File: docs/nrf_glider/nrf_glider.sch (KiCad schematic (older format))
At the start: 25 parts

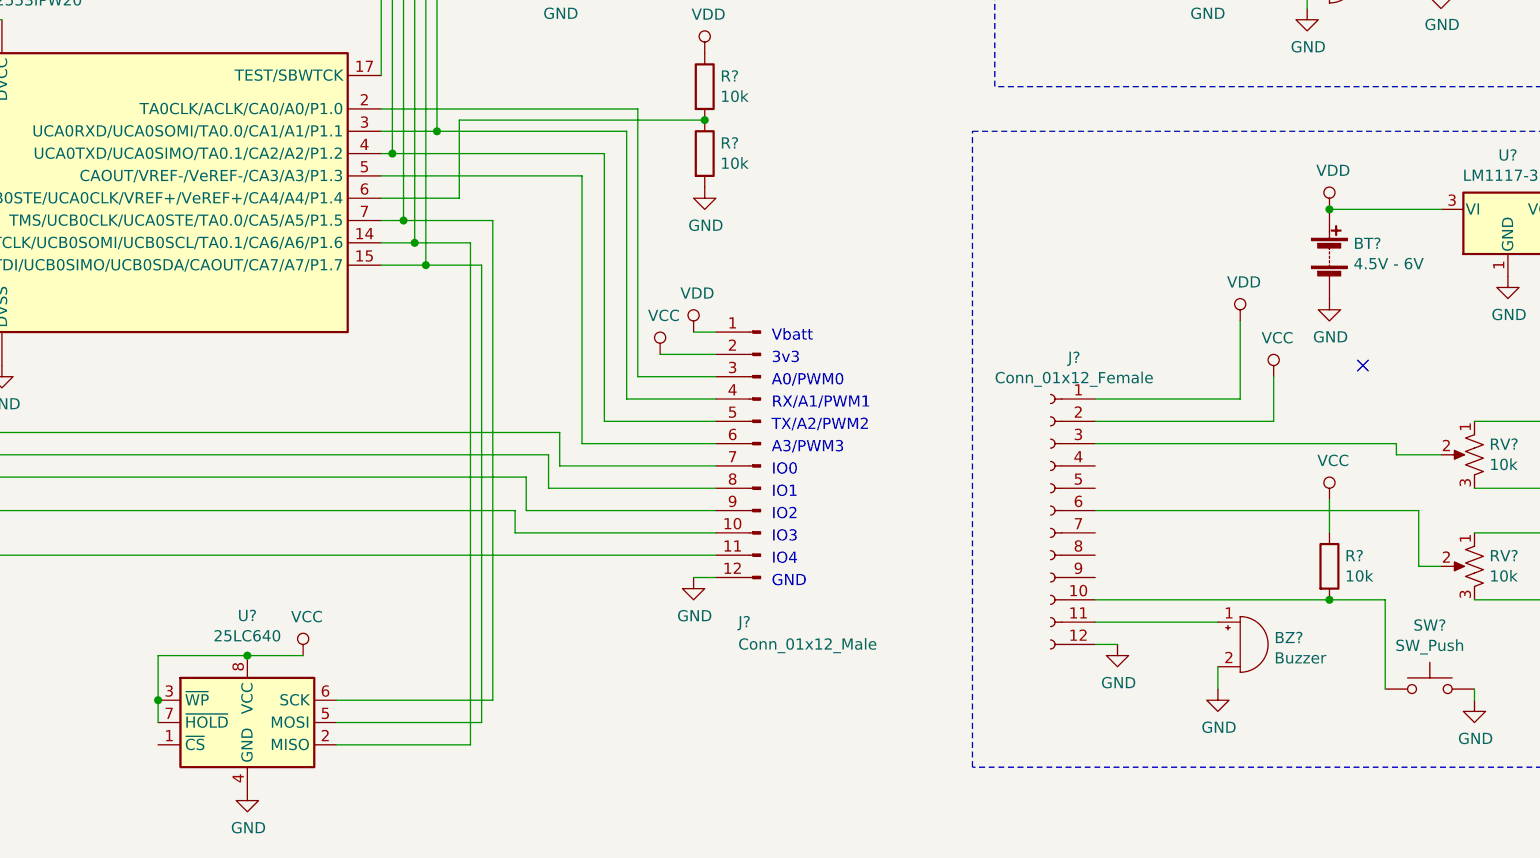
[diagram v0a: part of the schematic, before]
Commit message: add CS for eeprom, add UART connector on TX module
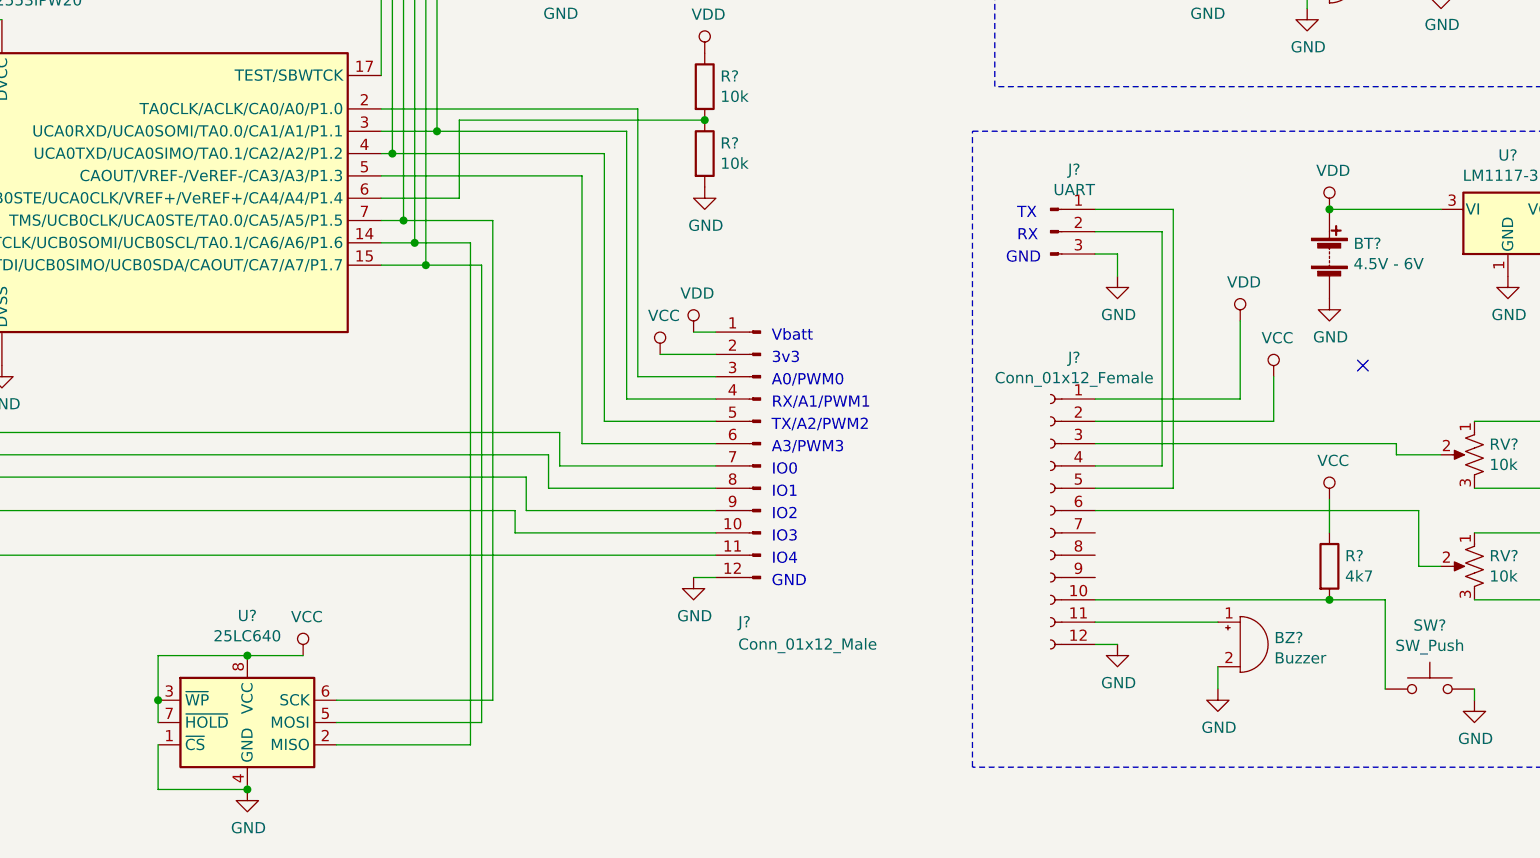
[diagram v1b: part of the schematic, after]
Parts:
- added J?: UART, symbol Connector:Conn_01x03_Male
- R?: value 10k -> 4k7
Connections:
- net GND: now also U?.1 (~CS), J?.3 (Pin_3)
- net at J?.4 (Pin_4): now also J?.2 (Pin_2)
- net at J?.5 (Pin_5): now also J?.1 (Pin_1)
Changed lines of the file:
@@
 EESchema Schematic File Version 4
+LIBS:nrf_glider-cache
 EELAYER 26 0
 EELAYER END
@@
 P 8800 5550
 F 0 "R?" H 8870 5596 50  0000 L CNN
-F 1 "10k" H 8870 5505 50  0000 L CNN
+F 1 "4k7" H 8870 5505 50  0000 L CNN
 F 2 "" V 8730 5550 50  0001 C CNN
 F 3 "~" H 8800 5550 50  0001 C CNN
@@
 Wire Wire Line
 	8800 5250 8800 5400
+$Comp
+L Connector:Conn_01x03_Male J?
+U 1 1 5BCF8F2B
+P 7550 4050
+F 0 "J?" H 7656 4328 50  0000 C CNN
+F 1 "UART" H 7656 4237 50  0000 C CNN
+F 2 "" H 7550 4050 50  0001 C CNN
+F 3 "~" H 7550 4050 50  0001 C CNN
+	1    7550 4050
+	1    0    0    -1
+$EndComp
+Wire Wire Line
+	7750 5100 8050 5100
+Wire Wire Line
+	8050 5100 8050 4050
+Wire Wire Line
+	8050 4050 7750 4050
+Wire Wire Line
+	7750 3950 8100 3950
+Wire Wire Line
+	8100 3950 8100 5200
+Wire Wire Line
+	8100 5200 7750 5200
+$Comp
+L power:GND #PWR?
+U 1 1 5BD038ED
+P 7850 4250
+F 0 "#PWR?" H 7850 4000 50  0001 C CNN
+F 1 "GND" H 7855 4077 50  0000 C CNN
+F 2 "" H 7850 4250 50  0001 C CNN
+F 3 "" H 7850 4250 50  0001 C CNN
+	1    7850 4250
+	1    0    0    -1
+$EndComp
+Wire Wire Line
+	7750 4150 7850 4150
+Wire Wire Line
+	7850 4150 7850 4250
+Text Notes 7400 4000 0    50   ~ 0
+TX
+Text Notes 7400 4100 0    50   ~ 0
+RX
+Text Notes 7350 4200 0    50   ~ 0
+GND
+Wire Wire Line
+	3550 6350 3550 6550
+Wire Wire Line
+	3550 6550 3950 6550
+Connection ~ 3950 6550
 $EndSCHEMATC

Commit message: tweaks to schematic
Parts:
- BT1, BT2: renamed from BT?; value 4.5V - 6V -> 4.5V - 9.9V
- M1: renamed from M?; value Motor_Servo -> Servo Left
- M2: renamed from M?; value Motor_Servo -> Servo Right
- R1: renamed from R?; value 10k -> 20k
- SW1: renamed from SW?; value SW_Push -> TRIM
- gave numbers to parts that had none: 20
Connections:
- net GND: no longer U2.1 (~CS)
- net at J2.7 (Pin_7), U1.18 (P2.7/XOUT): now also U2.1 (~CS)
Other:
- note added: "* IO0 shared with EEPROM chip select"
- note added: "23 October 2018"
- note added: "IO0*"
- note added: "Joystick"
- note added: "Left/Right\n"
- note added: "NRF and MSP430 based RC control"
- note added: "Up/Down"
- note added: "created by Toby Kurien"
- note removed: "IO0"
- moved on the sheet: R3

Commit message: added switch
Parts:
- added SW?: SW_SPST, symbol Switch:SW_SPST
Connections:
- net VDD: now also SW?.2 (B); no longer BT1.1 (+)
- new net: BT1.1 (+), SW?.1 (A)
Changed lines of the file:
@@
 	1    0    0    -1
 $EndComp
-Wire Wire Line
-	8800 3950 9300 3950
 $Comp
 L power:GND #PWR025
@@
 L power:VDD #PWR024
 U 1 1 5BD2C8A2
-P 8800 3950
-F 0 "#PWR024" H 8800 3800 50  0001 C CNN
-F 1 "VDD" H 8817 4123 50  0000 C CNN
-F 2 "" H 8800 3950 50  0001 C CNN
-F 3 "" H 8800 3950 50  0001 C CNN
-	1    8800 3950
-	1    0    0    -1
-$EndComp
-Connection ~ 8800 3950
+P 9300 3850
+F 0 "#PWR024" H 9300 3700 50  0001 C CNN
+F 1 "VDD" H 9317 4023 50  0000 C CNN
+F 2 "" H 9300 3850 50  0001 C CNN
+F 3 "" H 9300 3850 50  0001 C CNN
+	1    9300 3850
+	1    0    0    -1
+$EndComp
 Wire Wire Line
 	10450 3950 10450 4000
@@
 	8500 5700 9050 5700
 Wire Wire Line
-	3950 5950 4200 5950
-Wire Wire Line
-	3550 5950 3950 5950
-Connection ~ 3950 5950
-Connection ~ 3550 6150
-Wire Wire Line
-	3550 6150 3550 5950
-Wire Wire Line
-	3550 6250 3550 6150
-Wire Wire Line
 	3550 6350 1150 6350
 Wire Wire Line
@@
 Text Notes 10300 7350 0    50   ~ 0
 created by Toby Kurien
+$Comp
+L Switch:SW_SPST SW?
+U 1 1 5BD0D3D1
+P 9000 3950
+F 0 "SW?" H 9000 4185 50  0000 C CNN
+F 1 "SW_SPST" H 9000 4094 50  0000 C CNN
+F 2 "" H 9000 3950 50  0001 C CNN
+F 3 "" H 9000 3950 50  0001 C CNN
+	1    9000 3950
+	1    0    0    -1
+$EndComp
+Wire Wire Line
+	9200 3950 9300 3950
+Wire Wire Line
+	9300 3850 9300 3950
+Connection ~ 9300 3950
+Wire Wire Line
+	3550 6250 3550 6150
+Wire Wire Line
+	3550 6150 3550 5950
+Connection ~ 3550 6150
+Connection ~ 3950 5950
+Wire Wire Line
+	3550 5950 3950 5950
+Wire Wire Line
+	3950 5950 4200 5950
 $EndSCHEMATC

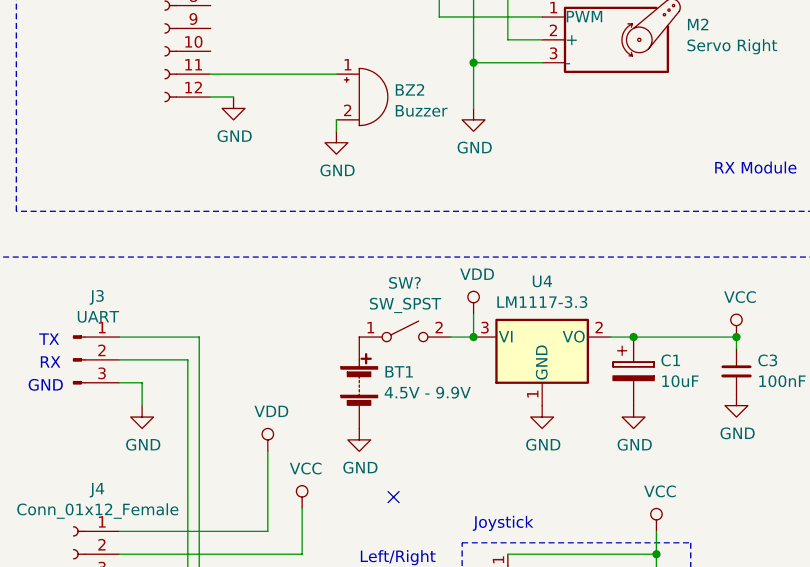
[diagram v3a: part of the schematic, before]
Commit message: Added some footprints
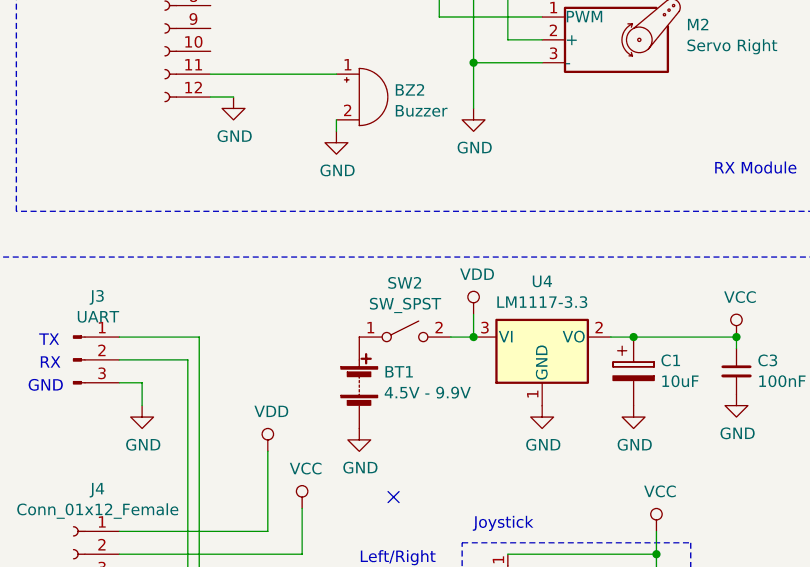
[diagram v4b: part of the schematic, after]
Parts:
- BT1, BT2: footprint (none) -> Connector_PinHeader_2.54mm:PinHeader_1x02_P2.54mm_Vertical
- BZ1, BZ2: footprint (none) -> Buzzer_Beeper:Buzzer_15x7.5RM7.6
- C1, C2: footprint (none) -> Capacitor_THT:CP_Radial_D8.0mm_P2.50mm
- C3, C4: footprint (none) -> Capacitor_THT:C_Disc_D5.0mm_W2.5mm_P5.00mm
- J1: footprint (none) -> Connector_PinHeader_2.54mm:PinHeader_1x06_P2.54mm_Vertical
- J2, J4, J5: footprint (none) -> Connector_PinHeader_2.54mm:PinHeader_1x12_P2.54mm_Vertical
- J3: footprint (none) -> Connector_PinHeader_2.54mm:PinHeader_1x03_P2.54mm_Horizontal
- M1, M2: footprint (none) -> Connector_PinHeader_2.54mm:PinHeader_1x03_P2.54mm_Vertical
- R1, R2, R3: footprint (none) -> Resistor_THT:R_Axial_DIN0411_L9.9mm_D3.6mm_P12.70mm_Horizontal
- RV1, RV2: footprint (none) -> Potentiometer_THT:Potentiometer_ACP_CA9-V10_Vertical
- SW1: footprint (none) -> Button_Switch_THT:SW_PUSH_6mm_H5mm
- U1: footprint Package_SO:TSSOP-20_4.4x6.5mm_P0.65mm -> Package_DIP:DIP-20_W7.62mm
- U2: footprint (none) -> Package_DIP:DIP-8_W7.62mm
- gave numbers to parts that had none: 1
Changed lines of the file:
@@
 F 0 "U1" H 2850 4878 50  0000 C CNN
 F 1 "MSP430G2553IPW20" H 2850 4787 50  0000 C CNN
-F 2 "Package_SO:TSSOP-20_4.4x6.5mm_P0.65mm" H 1400 3350 50  0001 C CIN
+F 2 "Package_DIP:DIP-20_W7.62mm" H 1400 3350 50  0001 C CIN
 F 3 "http://www.ti.com/lit/ds/symlink/msp430g2553.pdf" H 2800 3900 50  0001 C CNN
 	1    2850 3900
@@
 F 0 "U2" H 3950 6728 50  0000 C CNN
 F 1 "25LC640" H 3950 6637 50  0000 C CNN
-F 2 "" H 3950 6250 50  0001 C CNN
+F 2 "Package_DIP:DIP-8_W7.62mm" H 3950 6250 50  0001 C CNN
 F 3 "http://ww1.microchip.com/downloads/en/DeviceDoc/21832H.pdf" H 3950 6250 50  0001 C CNN
 	1    3950 6250
@@
 F 0 "BT2" H 9058 1246 50  0000 L CNN
 F 1 "4.5V - 9.9V" H 9058 1155 50  0000 L CNN
-F 2 "" V 8950 1260 50  0001 C CNN
+F 2 "Connector_PinHeader_2.54mm:PinHeader_1x02_P2.54mm_Vertical" V 8950 1260 50  0001 C CNN
 F 3 "~" V 8950 1260 50  0001 C CNN
 	1    8950 1200
@@
 F 0 "C4" H 10692 1196 50  0000 L CNN
 F 1 "100nF" H 10692 1105 50  0000 L CNN
-F 2 "" H 10600 1150 50  0001 C CNN
+F 2 "Capacitor_THT:C_Disc_D5.0mm_W2.5mm_P5.00mm" H 10600 1150 50  0001 C CNN
 F 3 "~" H 10600 1150 50  0001 C CNN
 	1    10600 1150
@@
 F 0 "C2" H 10268 1196 50  0000 L CNN
 F 1 "10uF" H 10268 1105 50  0000 L CNN
-F 2 "" H 10188 1000 50  0001 C CNN
+F 2 "Capacitor_THT:CP_Radial_D8.0mm_P2.50mm" H 10188 1000 50  0001 C CNN
 F 3 "~" H 10150 1150 50  0001 C CNN
 	1    10150 1150
@@
 F 0 "R1" H 6070 3446 50  0000 L CNN
 F 1 "20k" H 6070 3355 50  0000 L CNN
-F 2 "" V 5930 3400 50  0001 C CNN
+F 2 "Resistor_THT:R_Axial_DIN0411_L9.9mm_D3.6mm_P12.70mm_Horizontal" V 5930 3400 50  0001 C CNN
 F 3 "~" H 6000 3400 50  0001 C CNN
 	1    6000 3400
@@
 F 0 "R2" H 6070 3746 50  0000 L CNN
 F 1 "10k" H 6070 3655 50  0000 L CNN
-F 2 "" V 5930 3700 50  0001 C CNN
+F 2 "Resistor_THT:R_Axial_DIN0411_L9.9mm_D3.6mm_P12.70mm_Horizontal" V 5930 3700 50  0001 C CNN
 F 3 "~" H 6000 3700 50  0001 C CNN
 	1    6000 3700
@@
 F 0 "J2" H 6350 4200 50  0000 R CNN
 F 1 "Conn_01x12_Male" H 6350 4100 50  0000 R CNN
-F 2 "" H 6250 5000 50  0001 C CNN
+F 2 "Connector_PinHeader_2.54mm:PinHeader_1x12_P2.54mm_Vertical" H 6250 5000 50  0001 C CNN
 F 3 "~" H 6250 5000 50  0001 C CNN
 	1    6250 5000
@@
 F 0 "J5" H 7844 2985 50  0000 C CNN
 F 1 "Conn_01x12_Female" H 7844 2894 50  0000 C CNN
-F 2 "" H 7950 2300 50  0001 C CNN
+F 2 "Connector_PinHeader_2.54mm:PinHeader_1x12_P2.54mm_Vertical" H 7950 2300 50  0001 C CNN
 F 3 "~" H 7950 2300 50  0001 C CNN
 	1    7950 2300
@@
 F 0 "J4" H 7444 5985 50  0000 C CNN
 F 1 "Conn_01x12_Female" H 7444 5894 50  0000 C CNN
-F 2 "" H 7550 5300 50  0001 C CNN
+F 2 "Connector_PinHeader_2.54mm:PinHeader_1x12_P2.54mm_Vertical" H 7550 5300 50  0001 C CNN
 F 3 "~" H 7550 5300 50  0001 C CNN
 	1    7550 5300
@@
 F 0 "M1" H 10231 2215 50  0000 L CNN
 F 1 "Servo Left" H 10231 2124 50  0000 L CNN
-F 2 "" H 9900 1960 50  0001 C CNN
+F 2 "Connector_PinHeader_2.54mm:PinHeader_1x03_P2.54mm_Vertical" H 9900 1960 50  0001 C CNN
 F 3 "http://forums.parallax.com/uploads/attachments/46831/74481.png" H 9900 1960 50  0001 C CNN
 	1    9900 2150
@@
 F 0 "M2" H 10231 2715 50  0000 L CNN
 F 1 "Servo Right" H 10231 2624 50  0000 L CNN
-F 2 "" H 9900 2460 50  0001 C CNN
+F 2 "Connector_PinHeader_2.54mm:PinHeader_1x03_P2.54mm_Vertical" H 9900 2460 50  0001 C CNN
 F 3 "http://forums.parallax.com/uploads/attachments/46831/74481.png" H 9900 2460 50  0001 C CNN
 	1    9900 2650
@@
 F 0 "BZ2" H 8953 2929 50  0000 L CNN
 F 1 "Buzzer" H 8953 2838 50  0000 L CNN
-F 2 "" V 8775 3000 50  0001 C CNN
+F 2 "Buzzer_Beeper:Buzzer_15x7.5RM7.6" V 8775 3000 50  0001 C CNN
 F 3 "~" V 8775 3000 50  0001 C CNN
 	1    8800 2900
@@
 F 0 "RV1" H 9383 5096 50  0000 R CNN
 F 1 "10k" H 9383 5005 50  0000 R CNN
-F 2 "" H 9450 5050 50  0001 C CNN
+F 2 "Potentiometer_THT:Potentiometer_ACP_CA9-V10_Vertical" H 9450 5050 50  0001 C CNN
 F 3 "~" H 9450 5050 50  0001 C CNN
 	1    9450 5050
@@
 F 0 "RV2" H 9383 5596 50  0000 R CNN
 F 1 "10k" H 9383 5505 50  0000 R CNN
-F 2 "" H 9450 5550 50  0001 C CNN
+F 2 "Potentiometer_THT:Potentiometer_ACP_CA9-V10_Vertical" H 9450 5550 50  0001 C CNN
 F 3 "~" H 9450 5550 50  0001 C CNN
 	1    9450 5550
@@
 F 0 "BZ1" H 8553 5929 50  0000 L CNN
 F 1 "Buzzer" H 8553 5838 50  0000 L CNN
-F 2 "" V 8375 6000 50  0001 C CNN
+F 2 "Buzzer_Beeper:Buzzer_15x7.5RM7.6" V 8375 6000 50  0001 C CNN
 F 3 "~" V 8375 6000 50  0001 C CNN
 	1    8400 5900
@@
 F 0 "SW1" H 9250 6385 50  0000 C CNN
 F 1 "TRIM" H 9250 6294 50  0000 C CNN
-F 2 "" H 9250 6300 50  0001 C CNN
+F 2 "Button_Switch_THT:SW_PUSH_6mm_H5mm" H 9250 6300 50  0001 C CNN
 F 3 "" H 9250 6300 50  0001 C CNN
 	1    9250 6100
@@
 F 0 "BT1" H 8908 4196 50  0000 L CNN
 F 1 "4.5V - 9.9V" H 8908 4105 50  0000 L CNN
-F 2 "" V 8800 4210 50  0001 C CNN
+F 2 "Connector_PinHeader_2.54mm:PinHeader_1x02_P2.54mm_Vertical" V 8800 4210 50  0001 C CNN
 F 3 "~" V 8800 4210 50  0001 C CNN
 	1    8800 4150
@@
 F 0 "C3" H 10542 4146 50  0000 L CNN
 F 1 "100nF" H 10542 4055 50  0000 L CNN
-F 2 "" H 10450 4100 50  0001 C CNN
+F 2 "Capacitor_THT:C_Disc_D5.0mm_W2.5mm_P5.00mm" H 10450 4100 50  0001 C CNN
 F 3 "~" H 10450 4100 50  0001 C CNN
 	1    10450 4100
@@
 F 0 "C1" H 10118 4146 50  0000 L CNN
 F 1 "10uF" H 10118 4055 50  0000 L CNN
-F 2 "" H 10038 3950 50  0001 C CNN
+F 2 "Capacitor_THT:CP_Radial_D8.0mm_P2.50mm" H 10038 3950 50  0001 C CNN
 F 3 "~" H 10000 4100 50  0001 C CNN
 	1    10000 4100
@@
 F 0 "J1" H 6250 650 50  0000 R CNN
 F 1 "PROG" H 6250 550 50  0000 R CNN
-F 2 "" H 6150 1050 50  0001 C CNN
+F 2 "Connector_PinHeader_2.54mm:PinHeader_1x06_P2.54mm_Vertical" H 6150 1050 50  0001 C CNN
 F 3 "~" H 6150 1050 50  0001 C CNN
 	1    6150 1050
@@
 F 0 "R3" H 8570 5546 50  0000 L CNN
 F 1 "4k7" H 8570 5455 50  0000 L CNN
-F 2 "" V 8430 5500 50  0001 C CNN
+F 2 "Resistor_THT:R_Axial_DIN0411_L9.9mm_D3.6mm_P12.70mm_Horizontal" V 8430 5500 50  0001 C CNN
 F 3 "~" H 8500 5500 50  0001 C CNN
 	1    8500 5500
@@
 F 0 "J3" H 7656 4328 50  0000 C CNN
 F 1 "UART" H 7656 4237 50  0000 C CNN
-F 2 "" H 7550 4050 50  0001 C CNN
+F 2 "Connector_PinHeader_2.54mm:PinHeader_1x03_P2.54mm_Horizontal" H 7550 4050 50  0001 C CNN
 F 3 "~" H 7550 4050 50  0001 C CNN
 	1    7550 4050
@@
 created by Toby Kurien
 $Comp
-L Switch:SW_SPST SW?
+L Switch:SW_SPST SW2
 U 1 1 5BD0D3D1
 P 9000 3950
-F 0 "SW?" H 9000 4185 50  0000 C CNN
+F 0 "SW2" H 9000 4185 50  0000 C CNN
 F 1 "SW_SPST" H 9000 4094 50  0000 C CNN
 F 2 "" H 9000 3950 50  0001 C CNN
